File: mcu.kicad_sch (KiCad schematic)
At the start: 33 parts, among them J4 Conn_01x10, J5 Conn_01x10, J6 Conn_02x05_Odd_Even, J7 Conn_01x05_Pin, U7 REF3033, U8 STM32F407VGTx, Y1 8MHz

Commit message: sch: Update Title Block Info - rev0.3 -> rev0_3 - Correct the title of each schematics - Update the modified time
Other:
- company: M-Labs -> M-Labs Limited
- title: Kirdy -> MCU
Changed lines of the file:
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@@
   (paper "A3")
   (title_block
-    (title "Kirdy")
-    (date "2022-07-03")
-    (rev "r0.3")
-    (company "M-Labs")
+    (title "MCU")
+    (date "2023-11-09")
+    (rev "r0_3")
+    (company "M-Labs Limited")
     (comment 1 "Linus Woo Chun Kit")
   )

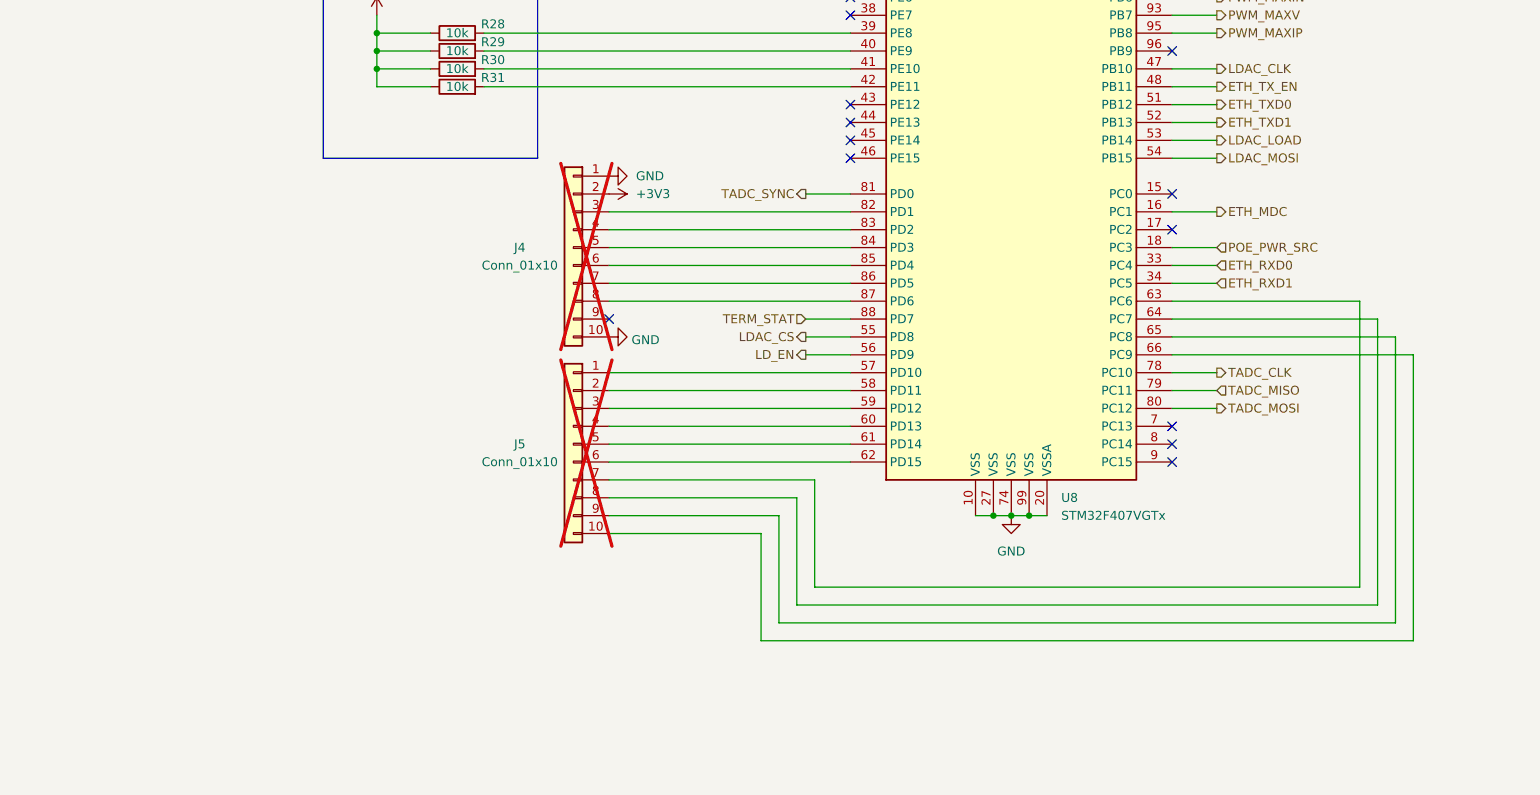
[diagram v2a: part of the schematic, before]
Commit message: sch, pcb: Add 12V & Mounting holes to MCU EXT HDR
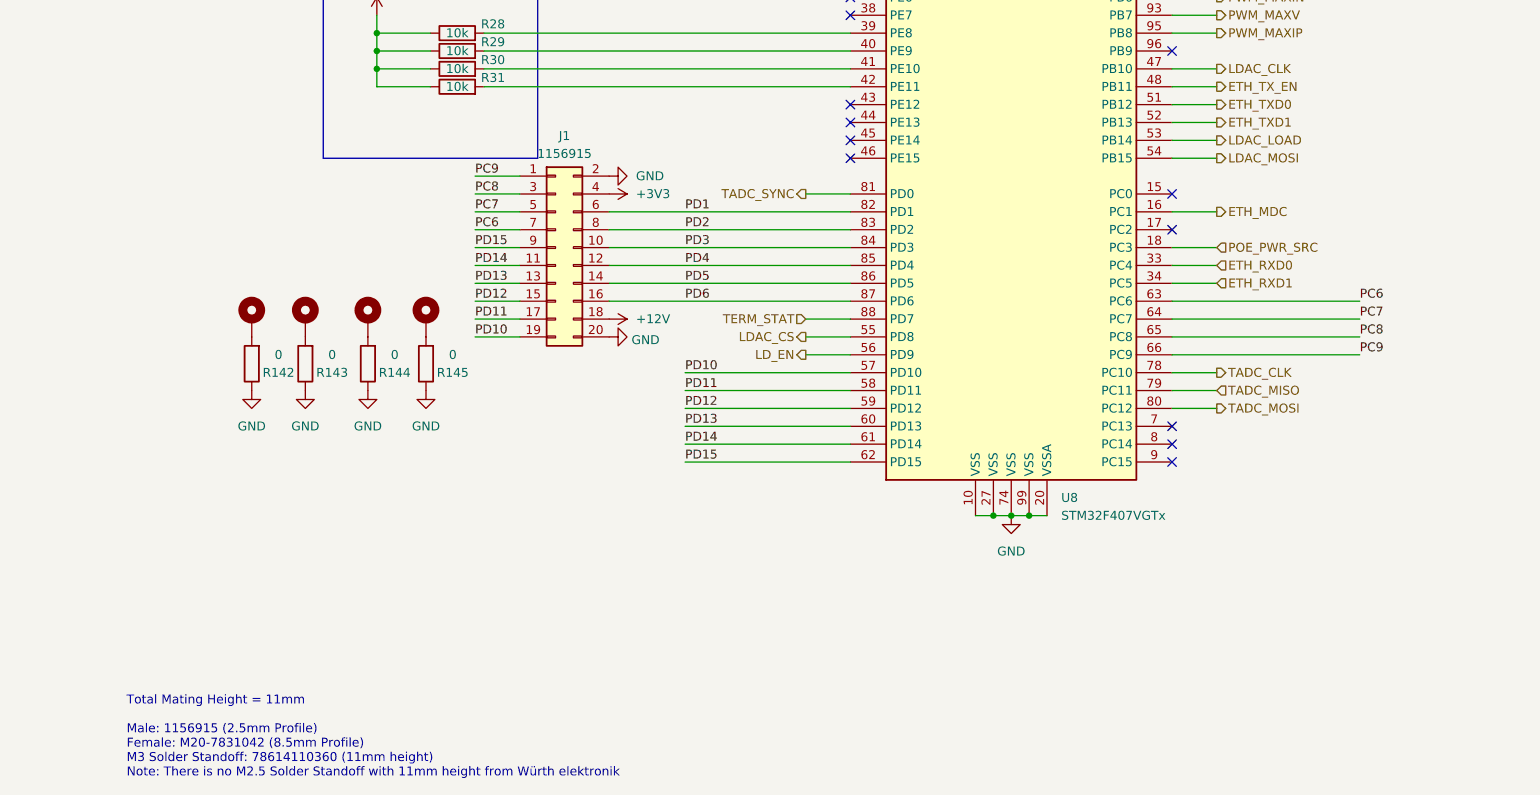
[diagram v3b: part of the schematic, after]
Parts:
- removed J4, J5: Conn_01x10, Connector_PinHeader_2.54mm:PinHeader_1x10_P2.54mm_Vertical, symbol Connector_Generic:Conn_01x10
- added H5, H6, H7, H8: 78614110360, Mounting_Wuerth:Mounting_Wuerth_WA-SMSI-M3_H11mm_9774110360, symbol Mechanical:MountingHole_Pad
- added J1: 1156915, kirdy:1156915, symbol Connector_Generic:Conn_02x10_Odd_Even
- added R142, R143, R144, R145: 0, Resistor_SMD:R_0603_1608Metric, symbol Device:R
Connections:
- net +3V3: now also J1.4 (Pin_4)
- net GND: now also J1.2 (Pin_2), J1.20 (Pin_20), R142.1, R143.1, R144.1, R145.1
- net PD1: now reaches U8.82 (PD1)
- net PD1: now also J1.6 (Pin_6)
- net PD2: now reaches U8.83 (PD2)
- net PD2: now also J1.8 (Pin_8)
- net PD3: now reaches U8.84 (PD3)
- net PD3: now also J1.10 (Pin_10)
- net PD4: now reaches U8.85 (PD4)
- net PD4: now also J1.12 (Pin_12)
- net PD5: now reaches U8.86 (PD5)
- net PD5: now also J1.14 (Pin_14)
- net PD6: now reaches U8.87 (PD6)
- net PD6: now also J1.16 (Pin_16)
- net PD10: now reaches U8.57 (PD10)
- net PD10: now also J1.19 (Pin_19)
- net PD11: now reaches U8.58 (PD11)
- net PD11: now also J1.17 (Pin_17)
- net PD12: now reaches U8.59 (PD12)
- net PD12: now also J1.15 (Pin_15)
- net PD13: now reaches U8.60 (PD13)
- net PD13: now also J1.13 (Pin_13)
- net PD14: now reaches U8.61 (PD14)
- net PD14: now also J1.11 (Pin_11)
- net PD15: now reaches U8.62 (PD15)
- net PD15: now also J1.9 (Pin_9)
- net PC6: now reaches U8.63 (PC6)
- net PC6: now also J1.7 (Pin_7)
- net PC7: now reaches U8.64 (PC7)
- net PC7: now also J1.5 (Pin_5)
- net PC8: now reaches U8.65 (PC8)
- net PC8: now also J1.3 (Pin_3)
- net PC9: now reaches U8.66 (PC9)
- net PC9: now also J1.1 (Pin_1)
- new net: H6.1, R143.2
- new net: H5.1, R142.2
- new net: H7.1, R144.2
- new net: H8.1, R145.2
- new net +12V: J1.18 (Pin_18)
- no-connect marks 26 -> 25
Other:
- note added: "Total Mating Height = 11mm Male: 1156915 (2.5mm Profile) Female: M20-7831042 (8.5mm Profile) M3 Solder Standoff: 78614110360 (11mm height) Note: There is no M2.5 Solder Standoff with 11mm height from Würth elektronik"

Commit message: Cleanup and Update Modification Date
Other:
- note added: "Total Mating Height = 11mm Male: 1156915 (2.5mm Profile) Female: M20-7831042 (8.5mm Profile) M3 Solder Standoff: 78614110360 (11mm height)"
- note removed: "Total Mating Height = 11mm Male: 1156915 (2.5mm Profile) Female: M20-7831042 (8.5mm Profile) M3 Solder Standoff: 78614110360 (11mm height) Note: There is no M2.5 Solder Standoff with 11mm height from Würth elektronik"
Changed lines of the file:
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@@
   (title_block
     (title "MCU")
-    (date "2023-11-09")
+    (date "2023-11-27")
     (rev "r0_3")
     (company "M-Labs Limited")
@@
     (stroke (width 0) (type default))
   )
-  (polyline (pts (xy 105.41 162.56) (xy 135.89 162.56))
+  (polyline (pts (xy 107.95 154.94) (xy 138.43 154.94))
     (stroke (width 0) (type default))
   )
@@
     (stroke (width 0) (type default))
   )
-  (polyline (pts (xy 135.89 162.56) (xy 135.89 134.62))
+  (polyline (pts (xy 138.43 154.94) (xy 138.43 134.62))
     (stroke (width 0) (type default))
   )
@@
     (stroke (width 0) (type default))
   )
-  (polyline (pts (xy 105.41 134.62) (xy 105.41 162.56))
+  (polyline (pts (xy 107.95 134.62) (xy 107.95 154.94))
     (stroke (width 0) (type default))
   )
@@
     (stroke (width 0) (type default))
   )
-  (polyline (pts (xy 105.41 134.62) (xy 135.89 134.62))
+  (polyline (pts (xy 107.95 134.62) (xy 138.43 134.62))
     (stroke (width 0) (type default))
   )
@@
     (stroke (width 0) (type default))
   )
-  (text "Revision\n" (at 123.19 139.7 0)
+  (text "Revision\n" (at 121.285 138.43 0)
     (effects (font (size 1.27 1.27)) (justify left bottom))
   )
-  (text "Total Mating Height = 11mm\n\nMale: 1156915 (2.5mm Profile)\nFemale: M20-7831042 (8.5mm Profile)\nM3 Solder Standoff: 78614110360 (11mm height)\nNote: There is no M2.5 Solder Standoff with 11mm height from Würth elektronik\n\n"
-    (at 77.47 252.73 0)
+  (text "Total Mating Height = 11mm\n\nMale: 1156915 (2.5mm Profile)\nFemale: M20-7831042 (8.5mm Profile)\nM3 Solder Standoff: 78614110360 (11mm height)\n"
+    (at 76.2 180.34 0)
     (effects (font (size 1.27 1.27)) (justify left bottom))
   )

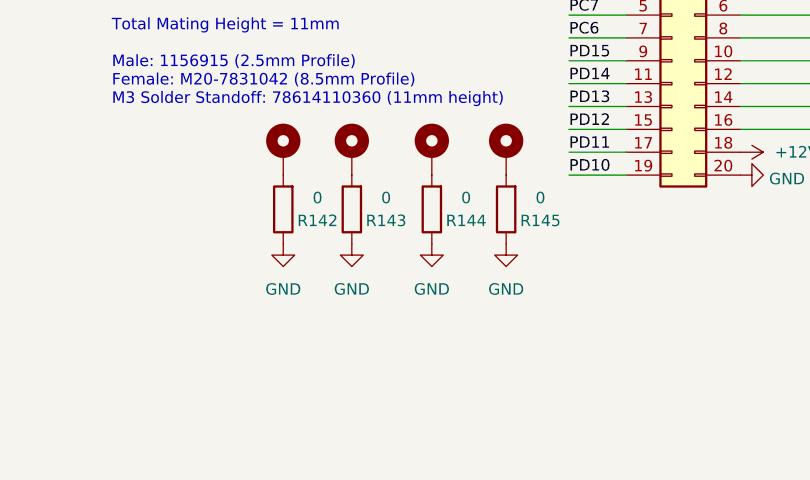
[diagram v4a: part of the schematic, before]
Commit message: sch: Add Mounting Screw Symbol and MFR/PN
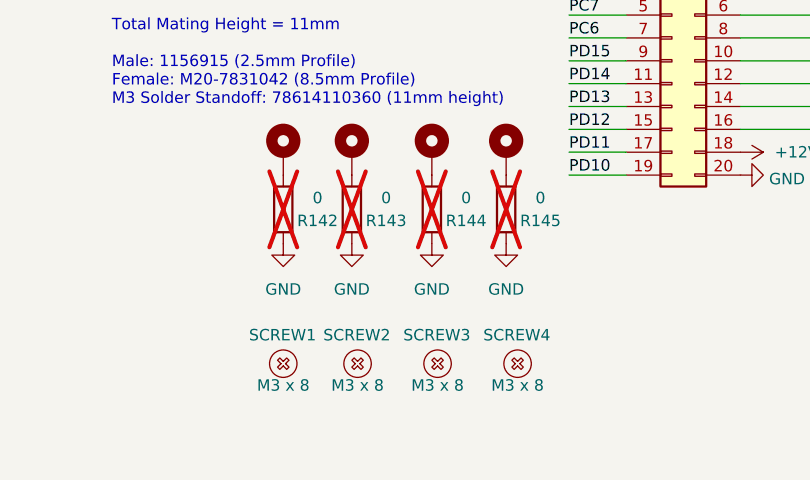
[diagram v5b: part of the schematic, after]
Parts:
- added SCREW1, SCREW2, SCREW3, SCREW4: M3 x 8, symbol kirdy:Screw
- R142, R143, R144, R145: now not fitted
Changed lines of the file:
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@@
   )
   (symbol (lib_id "Device:R") (at 102.87 191.77 180) (unit 1)
-    (in_bom yes) (on_board yes) (dnp no)
+    (in_bom yes) (on_board yes) (dnp yes)
     (property "Reference" "R143" (at 106.68 193.04 0)
       (effects (font (size 1.27 1.27)))
@@
   )
   (symbol (lib_id "Device:R") (at 95.25 191.77 180) (unit 1)
-    (in_bom yes) (on_board yes) (dnp no)
+    (in_bom yes) (on_board yes) (dnp yes)
     (property "Reference" "R142" (at 99.06 193.04 0)
       (effects (font (size 1.27 1.27)))
@@
     )
   )
+  (symbol (lib_id "kirdy:Screw") (at 103.505 208.915 0) (unit 1)
+    (in_bom yes) (on_board no) (dnp no)
+    (property "Reference" "SCREW2" (at 99.695 205.74 0)
+      (effects (font (size 1.27 1.27)) (justify left))
+    )
+    (property "Value" "M3 x 8" (at 103.505 211.328 0)
+      (effects (font (size 1.27 1.27)))
+    )
+    (property "Footprint" "" (at 102.235 207.645 0)
+      (effects (font (size 1.27 1.27)) hide)
+    )
+    (property "Datasheet" "" (at 102.235 207.645 0)
+      (effects (font (size 1.27 1.27)) hide)
+    )
+    (property "MFR_PN" "FH4-M3-8" (at 103.505 208.915 0)
+      (effects (font (size 1.27 1.27)) hide)
+    )
+    (instances
+      (project "kirdy"
+        (path "/88da1dd8-9274-4b55-84fb-90006c9b6e8f"
+          (reference "SCREW2") (unit 1)
+        )
+        (path "/88da1dd8-9274-4b55-84fb-90006c9b6e8f/e9afb2cc-7f7f-4cb9-888a-0bfd71b1d070"
+          (reference "SCREW6") (unit 1)
+        )
+      )
+    )
+  )
   (symbol (lib_id "Device:C") (at 204.47 41.91 0) (unit 1)
     (in_bom yes) (on_board yes) (dnp no) (fields_autoplaced)
@@
   )
   (symbol (lib_id "Device:R") (at 111.76 191.77 180) (unit 1)
-    (in_bom yes) (on_board yes) (dnp no)
+    (in_bom yes) (on_board yes) (dnp yes)
     (property "Reference" "R144" (at 115.57 193.04 0)
       (effects (font (size 1.27 1.27)))
@@
     )
   )
+  (symbol (lib_id "kirdy:Screw") (at 95.25 208.915 0) (unit 1)
+    (in_bom yes) (on_board no) (dnp no)
+    (property "Reference" "SCREW1" (at 91.44 205.74 0)
+      (effects (font (size 1.27 1.27)) (justify left))
+    )
+    (property "Value" "M3 x 8" (at 95.25 211.328 0)
+      (effects (font (size 1.27 1.27)))
+    )
+    (property "Footprint" "" (at 93.98 207.645 0)
+      (effects (font (size 1.27 1.27)) hide)
+    )
+    (property "Datasheet" "" (at 93.98 207.645 0)
+      (effects (font (size 1.27 1.27)) hide)
+    )
+    (property "MFR_PN" "FH4-M3-8" (at 95.25 208.915 0)
+      (effects (font (size 1.27 1.27)) hide)
+    )
+    (instances
+      (project "kirdy"
+        (path "/88da1dd8-9274-4b55-84fb-90006c9b6e8f"
+          (reference "SCREW1") (unit 1)
+        )
+        (path "/88da1dd8-9274-4b55-84fb-90006c9b6e8f/e9afb2cc-7f7f-4cb9-888a-0bfd71b1d070"
+          (reference "SCREW5") (unit 1)
+        )
+      )
+    )
+  )
   (symbol (lib_id "power:+5VA") (at 72.39 85.725 0) (unit 1)
     (in_bom yes) (on_board yes) (dnp no) (fields_autoplaced)
@@
     )
   )
+  (symbol (lib_id "kirdy:Screw") (at 121.285 208.915 0) (unit 1)
+    (in_bom yes) (on_board no) (dnp no)
+    (property "Reference" "SCREW4" (at 117.475 205.74 0)
+      (effects (font (size 1.27 1.27)) (justify left))
+    )
+    (property "Value" "M3 x 8" (at 121.285 211.328 0)
+      (effects (font (size 1.27 1.27)))
+    )
+    (property "Footprint" "" (at 120.015 207.645 0)
+      (effects (font (size 1.27 1.27)) hide)
+    )
+    (property "Datasheet" "" (at 120.015 207.645 0)
+      (effects (font (size 1.27 1.27)) hide)
+    )
+    (property "MFR_PN" "FH4-M3-8" (at 121.285 208.915 0)
+      (effects (font (size 1.27 1.27)) hide)
+    )
+    (instances
+      (project "kirdy"
+        (path "/88da1dd8-9274-4b55-84fb-90006c9b6e8f"
+          (reference "SCREW4") (unit 1)
+        )
+        (path "/88da1dd8-9274-4b55-84fb-90006c9b6e8f/e9afb2cc-7f7f-4cb9-888a-0bfd71b1d070"
+          (reference "SCREW8") (unit 1)
+        )
+      )
+    )
+  )
   (symbol (lib_id "Mechanical:MountingHole_Pad") (at 120.015 185.42 0) (unit 1)
     (in_bom yes) (on_board yes) (dnp no) (fields_autoplaced)
@@
         (path "/88da1dd8-9274-4b55-84fb-90006c9b6e8f/e9afb2cc-7f7f-4cb9-888a-0bfd71b1d070"
           (reference "#PWR059") (unit 1)
+        )
+      )
+    )
+  )
+  (symbol (lib_id "kirdy:Screw") (at 112.395 208.915 0) (unit 1)
+    (in_bom yes) (on_board no) (dnp no)
+    (property "Reference" "SCREW3" (at 108.585 205.74 0)
+      (effects (font (size 1.27 1.27)) (justify left))
+    )
+    (property "Value" "M3 x 8" (at 112.395 211.328 0)
+      (effects (font (size 1.27 1.27)))
+    )
+    (property "Footprint" "" (at 111.125 207.645 0)
+      (effects (font (size 1.27 1.27)) hide)
+    )
+    (property "Datasheet" "" (at 111.125 207.645 0)
+      (effects (font (size 1.27 1.27)) hide)
+    )
+    (property "MFR_PN" "FH4-M3-8" (at 112.395 208.915 0)
+      (effects (font (size 1.27 1.27)) hide)
+    )
+    (instances
+      (project "kirdy"
+        (path "/88da1dd8-9274-4b55-84fb-90006c9b6e8f"
+          (reference "SCREW3") (unit 1)
+        )
+        (path "/88da1dd8-9274-4b55-84fb-90006c9b6e8f/e9afb2cc-7f7f-4cb9-888a-0bfd71b1d070"
+          (reference "SCREW7") (unit 1)
         )
       )
@@
   )
   (symbol (lib_id "Device:R") (at 120.015 191.77 180) (unit 1)
-    (in_bom yes) (on_board yes) (dnp no)
+    (in_bom yes) (on_board yes) (dnp yes)
     (property "Reference" "R145" (at 123.825 193.04 0)
       (effects (font (size 1.27 1.27)))
